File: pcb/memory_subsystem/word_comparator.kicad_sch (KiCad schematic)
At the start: 6 parts, among them U13 74LS85, U14 74LS85, U15 74LS21

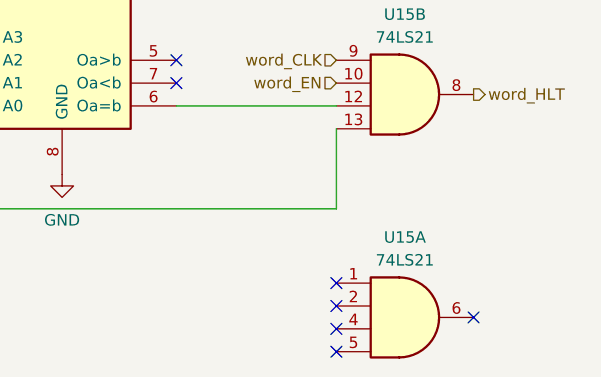
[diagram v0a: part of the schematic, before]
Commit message: Fixed spacing problem: no warnings/erros
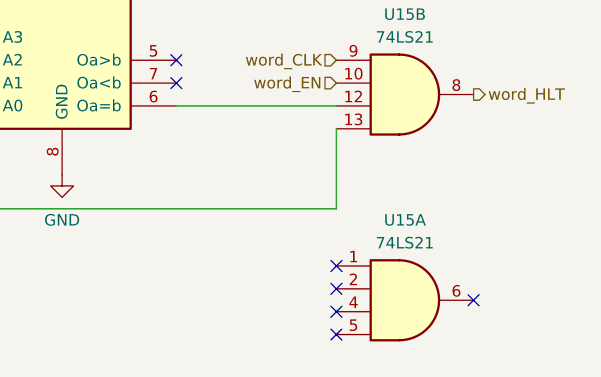
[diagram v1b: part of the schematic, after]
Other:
- moved on the sheet: U15A
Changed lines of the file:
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@@
 	)
 	(no_connect
-		(at 148.59 102.235)
+		(at 148.59 100.33)
 	)
 	(no_connect
-		(at 148.59 94.615)
+		(at 148.59 92.71)
 	)
 	(no_connect
@@
 	)
 	(no_connect
-		(at 148.59 99.695)
+		(at 148.59 97.79)
 	)
 	(no_connect
-		(at 163.83 98.425)
+		(at 163.83 96.52)
 	)
 	(no_connect
@@
 	)
 	(no_connect
-		(at 148.59 97.155)
+		(at 148.59 95.25)
 	)
 	(bus_entry
@@
 		(dnp no)
 		(fields_autoplaced yes)
-		(property "Reference" "#PWR063"
+		(property "Reference" "#PWR061"
 			(at 118.11 88.9 0)
 			(hide yes)
@@
 			(project "memory_subsystem"
 				(path "/eef9c2f8-b48e-448a-907d-9c9f187d4399/0e3afb8d-ff36-40e0-a62f-b04d75fffb8c"
-					(reference "#PWR063")
+					(reference "#PWR061")
 					(unit 1)
 				)
@@
 		(dnp no)
 		(fields_autoplaced yes)
-		(property "Reference" "#PWR067"
+		(property "Reference" "#PWR065"
 			(at 147.32 35.56 0)
 			(hide yes)
@@
 			(project "memory_subsystem"
 				(path "/eef9c2f8-b48e-448a-907d-9c9f187d4399/0e3afb8d-ff36-40e0-a62f-b04d75fffb8c"
-					(reference "#PWR067")
+					(reference "#PWR065")
 					(unit 1)
 				)
@@
 		(dnp no)
 		(fields_autoplaced yes)
-		(property "Reference" "#PWR062"
+		(property "Reference" "#PWR060"
 			(at 118.11 50.8 0)
 			(hide yes)
@@
 			(project "memory_subsystem"
 				(path "/eef9c2f8-b48e-448a-907d-9c9f187d4399/0e3afb8d-ff36-40e0-a62f-b04d75fffb8c"
-					(reference "#PWR062")
+					(reference "#PWR060")
 					(unit 1)
 				)
@@
 		(dnp no)
 		(fields_autoplaced yes)
-		(property "Reference" "#PWR069"
+		(property "Reference" "#PWR067"
 			(at 154.94 60.96 0)
 			(hide yes)
@@
 			(project "memory_subsystem"
 				(path "/eef9c2f8-b48e-448a-907d-9c9f187d4399/0e3afb8d-ff36-40e0-a62f-b04d75fffb8c"
-					(reference "#PWR069")
+					(reference "#PWR067")
 					(unit 1)
 				)
@@
 		(dnp no)
 		(fields_autoplaced yes)
-		(property "Reference" "#PWR055"
+		(property "Reference" "#PWR053"
 			(at 45.72 53.34 0)
 			(hide yes)
@@
 			(project "memory_subsystem"
 				(path "/eef9c2f8-b48e-448a-907d-9c9f187d4399/0e3afb8d-ff36-40e0-a62f-b04d75fffb8c"
-					(reference "#PWR055")
+					(reference "#PWR053")
 					(unit 1)
 				)
@@
 		(dnp no)
 		(fields_autoplaced yes)
-		(property "Reference" "#PWR056"
+		(property "Reference" "#PWR054"
 			(at 53.34 50.8 0)
 			(hide yes)
@@
 			(project "memory_subsystem"
 				(path "/eef9c2f8-b48e-448a-907d-9c9f187d4399/0e3afb8d-ff36-40e0-a62f-b04d75fffb8c"
-					(reference "#PWR056")
+					(reference "#PWR054")
 					(unit 1)
 				)
@@
 		(dnp no)
 		(fields_autoplaced yes)
-		(property "Reference" "#PWR061"
+		(property "Reference" "#PWR059"
 			(at 110.49 53.34 0)
 			(hide yes)
@@
 			(project "memory_subsystem"
 				(path "/eef9c2f8-b48e-448a-907d-9c9f187d4399/0e3afb8d-ff36-40e0-a62f-b04d75fffb8c"
-					(reference "#PWR061")
+					(reference "#PWR059")
 					(unit 1)
 				)
@@
 	(symbol
 		(lib_id "74xx:74LS21")
-		(at 156.21 98.425 0)
+		(at 156.21 96.52 0)
 		(unit 1)
 		(body_style 1)
@@
 		(fields_autoplaced yes)
 		(property "Reference" "U15"
-			(at 156.2003 89.535 0)
+			(at 156.2003 87.63 0)
 			(show_name no)
 			(do_not_autoplace no)
@@
 		)
 		(property "Value" "74LS21"
-			(at 156.2003 92.075 0)
+			(at 156.2003 90.17 0)
 			(show_name no)
 			(do_not_autoplace no)
@@
 		)
 		(property "Footprint" "Package_DIP:DIP-14_W7.62mm"
-			(at 156.21 98.425 0)
+			(at 156.21 96.52 0)
 			(hide yes)
 			(show_name no)
@@
 		)
 		(property "Datasheet" "http://www.ti.com/lit/gpn/sn74LS21"
-			(at 156.21 98.425 0)
+			(at 156.21 96.52 0)
 			(hide yes)
 			(show_name no)
@@
 		)
 		(property "Description" "Dual 4-input AND"
-			(at 156.21 98.425 0)
+			(at 156.21 96.52 0)
 			(hide yes)
 			(show_name no)
@@
 		(dnp no)
 		(fields_autoplaced yes)
-		(property "Reference" "#PWR058"
+		(property "Reference" "#PWR056"
 			(at 72.39 54.61 0)
 			(hide yes)
@@
 			(project "memory_subsystem"
 				(path "/eef9c2f8-b48e-448a-907d-9c9f187d4399/0e3afb8d-ff36-40e0-a62f-b04d75fffb8c"
-					(reference "#PWR058")
+					(reference "#PWR056")
 					(unit 1)
 				)
@@
 		(dnp no)
 		(fields_autoplaced yes)
-		(property "Reference" "#PWR066"
+		(property "Reference" "#PWR064"
 			(at 127 59.69 0)
 			(hide yes)
@@
 			(project "memory_subsystem"
 				(path "/eef9c2f8-b48e-448a-907d-9c9f187d4399/0e3afb8d-ff36-40e0-a62f-b04d75fffb8c"
-					(reference "#PWR066")
+					(reference "#PWR064")
 					(unit 1)
 				)
@@
 		(dnp no)
 		(fields_autoplaced yes)
-		(property "Reference" "#PWR065"
+		(property "Reference" "#PWR063"
 			(at 137.16 57.15 0)
 			(hide yes)
@@
 			(project "memory_subsystem"
 				(path "/eef9c2f8-b48e-448a-907d-9c9f187d4399/0e3afb8d-ff36-40e0-a62f-b04d75fffb8c"
-					(reference "#PWR065")
+					(reference "#PWR063")
 					(unit 1)
 				)
@@
 		(dnp no)
 		(fields_autoplaced yes)
-		(property "Reference" "#PWR060"
+		(property "Reference" "#PWR058"
 			(at 62.23 59.69 0)
 			(hide yes)
@@
 			(project "memory_subsystem"
 				(path "/eef9c2f8-b48e-448a-907d-9c9f187d4399/0e3afb8d-ff36-40e0-a62f-b04d75fffb8c"
-					(reference "#PWR060")
+					(reference "#PWR058")
 					(unit 1)
 				)
@@
 		(dnp no)
 		(fields_autoplaced yes)
-		(property "Reference" "#PWR057"
+		(property "Reference" "#PWR055"
 			(at 53.34 88.9 0)
 			(hide yes)
@@
 			(project "memory_subsystem"
 				(path "/eef9c2f8-b48e-448a-907d-9c9f187d4399/0e3afb8d-ff36-40e0-a62f-b04d75fffb8c"
-					(reference "#PWR057")
+					(reference "#PWR055")
 					(unit 1)
 				)
@@
 		(dnp no)
 		(fields_autoplaced yes)
-		(property "Reference" "#PWR068"
+		(property "Reference" "#PWR066"
 			(at 154.94 33.02 0)
 			(hide yes)
@@
 			(project "memory_subsystem"
 				(path "/eef9c2f8-b48e-448a-907d-9c9f187d4399/0e3afb8d-ff36-40e0-a62f-b04d75fffb8c"
-					(reference "#PWR068")
+					(reference "#PWR066")
 					(unit 1)
 				)
@@
 		(dnp no)
 		(fields_autoplaced yes)
-		(property "Reference" "#PWR064"
+		(property "Reference" "#PWR062"
 			(at 137.16 54.61 0)
 			(hide yes)
@@
 			(project "memory_subsystem"
 				(path "/eef9c2f8-b48e-448a-907d-9c9f187d4399/0e3afb8d-ff36-40e0-a62f-b04d75fffb8c"
-					(reference "#PWR064")
+					(reference "#PWR062")
 					(unit 1)
 				)
@@
 		(dnp no)
 		(fields_autoplaced yes)
-		(property "Reference" "#PWR059"
+		(property "Reference" "#PWR057"
 			(at 72.39 57.15 0)
 			(hide yes)
@@
 			(project "memory_subsystem"
 				(path "/eef9c2f8-b48e-448a-907d-9c9f187d4399/0e3afb8d-ff36-40e0-a62f-b04d75fffb8c"
-					(reference "#PWR059")
+					(reference "#PWR057")
 					(unit 1)
 				)
@@
 		)
 	)
-	(group ""
-		(members "4df121cb-a8d9-47d5-966e-266f92eaff76" "6f39a3b2-98e3-4352-9c0a-5c6ef771b37d"
-			"74de60b2-3b6f-4c4c-9145-51804617dd28" "c663b648-7136-49e1-92e6-b24abaf04bd9"
-			"ce98f19d-a8ce-4f94-99c0-a06bb35c9a9f"
-		)
-	)

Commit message: Tracks finished
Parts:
- C13, C14, C15: footprint Capacitor_SMD:C_0805_2012Metric -> Capacitor_SMD:C_0805_2012Metric_Pad1.18x1.45mm_HandSolder
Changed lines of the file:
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@@
 			)
 		)
-		(property "Footprint" "Capacitor_SMD:C_0805_2012Metric"
+		(property "Footprint" "Capacitor_SMD:C_0805_2012Metric_Pad1.18x1.45mm_HandSolder"
 			(at 53.34 46.0248 0)
 			(hide yes)
@@
 			)
 		)
-		(property "Footprint" "Capacitor_SMD:C_0805_2012Metric"
+		(property "Footprint" "Capacitor_SMD:C_0805_2012Metric_Pad1.18x1.45mm_HandSolder"
 			(at 154.94 28.2448 0)
 			(hide yes)
@@
 			)
 		)
-		(property "Footprint" "Capacitor_SMD:C_0805_2012Metric"
+		(property "Footprint" "Capacitor_SMD:C_0805_2012Metric_Pad1.18x1.45mm_HandSolder"
 			(at 118.11 46.0248 0)
 			(hide yes)
